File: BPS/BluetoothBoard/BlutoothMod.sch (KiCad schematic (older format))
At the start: 12 parts, among them SW2 SW_DIP_x01, U6 RN4870-V_RM118, U7 MCP100-315D

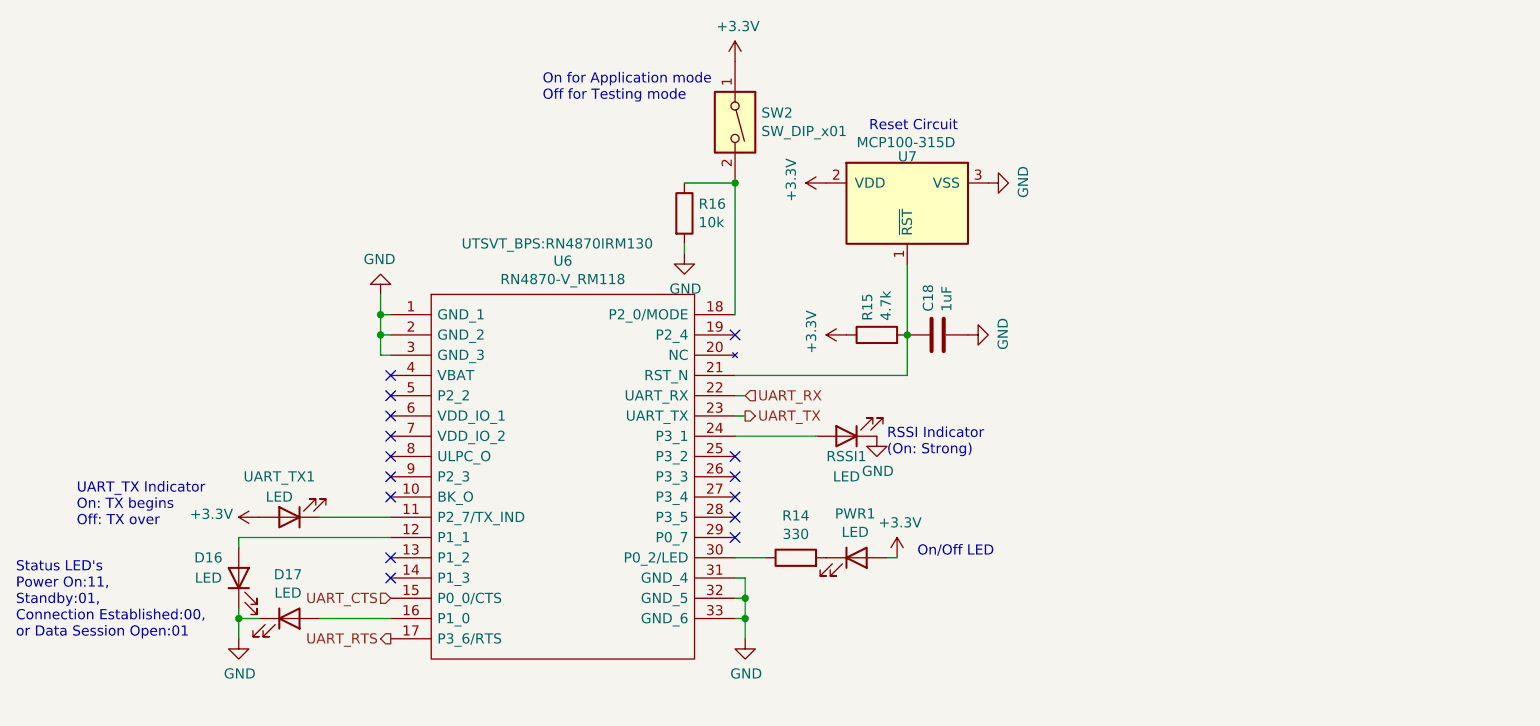
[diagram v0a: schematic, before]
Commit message: Created new board for Bluetooth module because the antenna cannot have a ground plane on it. Made everything connect using pin headers. Will mount the Bluetooth module board onto the Master board.
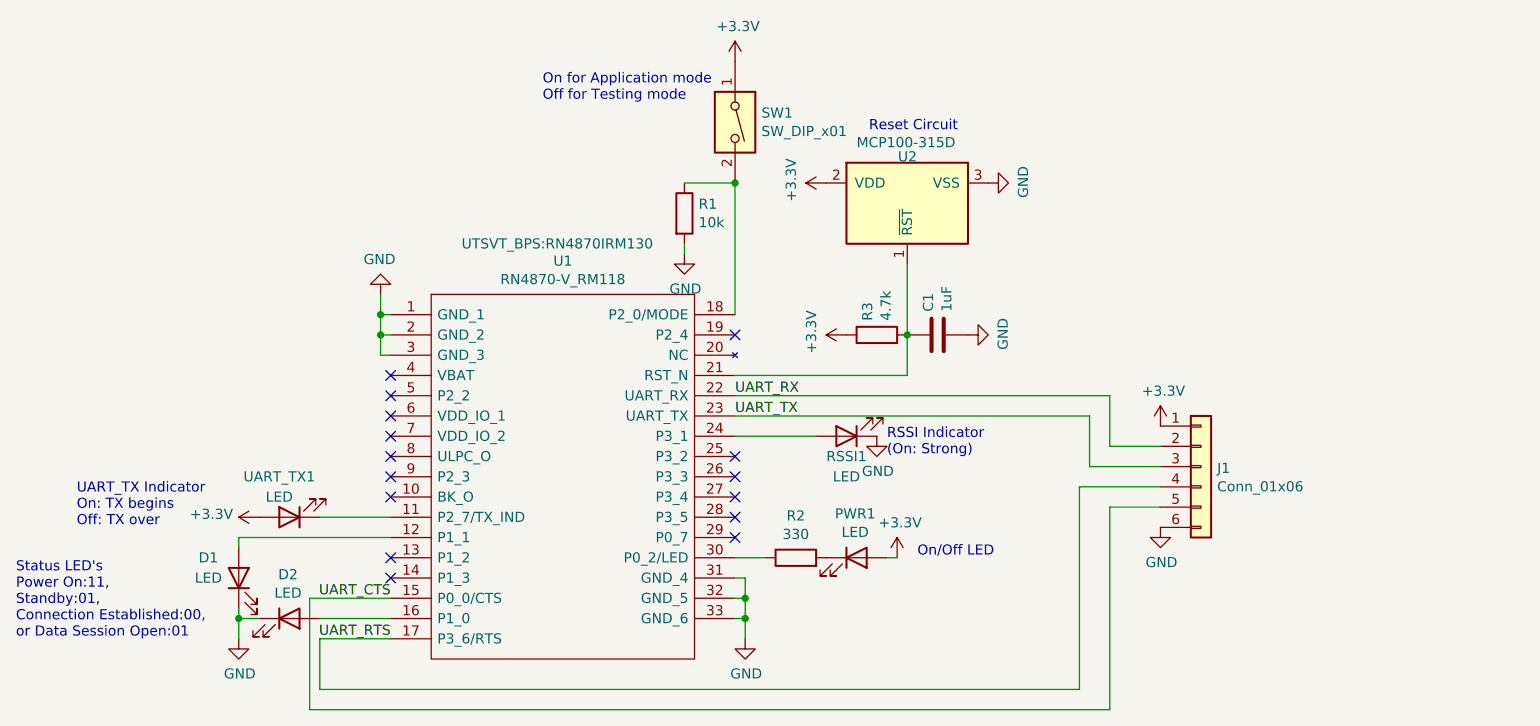
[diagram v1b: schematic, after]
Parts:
- added J1: Conn_01x06, Connector_PinHeader_2.54mm:PinHeader_1x06_P2.54mm_Vertical, symbol Connector_Generic:Conn_01x06
- renumbered C18 to C1, D16 to D1, D17 to D2, R16 to R1, R14 to R2, R15 to R3, SW2 to SW1, U6 to U1, U7 to U2
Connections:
- net +3V3: now also J1.1 (Pin_1)
- net GND: now also J1.6 (Pin_6)
- net UART_CTS: now also J1.5 (Pin_5)
- net UART_RTS: now also J1.4 (Pin_4)
- net UART_RX: now also J1.2 (Pin_2)
- net UART_TX: now also J1.3 (Pin_3)
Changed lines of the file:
@@
 $Descr A4 11693 8268
 encoding utf-8
-Sheet 11 11
+Sheet 1 1
 Title ""
 Date ""
@@
 $EndDescr
 $Comp
-L utsvt-bltmod:RN4870-V_RM118 U6
+L utsvt-bltmod:RN4870-V_RM118 U1
 U 1 1 5EE47912
 P 5000 2900
-F 0 "U6" H 5850 3165 50  0000 C CNN
+F 0 "U1" H 5850 3165 50  0000 C CNN
 F 1 "RN4870-V_RM118" H 5850 3074 50  0000 C CNN
 F 2 "UTSVT_BPS:RN4870IRM130" H 5350 3250 50  0000 L CNN
@@
 Connection ~ 6750 4400
 $Comp
-L power:GND #PWR0106
+L power:GND #PWR06
 U 1 1 5EE48E9A
 P 6750 4500
-F 0 "#PWR0106" H 6750 4250 50  0001 C CNN
+F 0 "#PWR06" H 6750 4250 50  0001 C CNN
 F 1 "GND" H 6755 4327 50  0000 C CNN
 F 2 "" H 6750 4500 50  0001 C CNN
@@
 Connection ~ 4950 2900
 $Comp
-L power:GND #PWR0107
+L power:GND #PWR03
 U 1 1 5EE4937A
 P 4950 2800
-F 0 "#PWR0107" H 4950 2550 50  0001 C CNN
+F 0 "#PWR03" H 4950 2550 50  0001 C CNN
 F 1 "GND" H 4955 2627 50  0000 C CNN
 F 2 "" H 4950 2800 50  0001 C CNN
@@
 $EndComp
 $Comp
-L power:+3.3V #PWR0112
+L power:+3.3V #PWR08
 U 1 1 5EE112CA
 P 7250 3000
-F 0 "#PWR0112" H 7250 2850 50  0001 C CNN
+F 0 "#PWR08" H 7250 2850 50  0001 C CNN
 F 1 "+3.3V" H 7265 3173 50  0000 C CNN
 F 2 "" H 7250 3000 50  0001 C CNN
@@
 $EndComp
 $Comp
-L Device:R R15
+L Device:R R3
 U 1 1 5EE108D1
 P 7400 3000
-F 0 "R15" H 7470 3046 50  0000 L CNN
+F 0 "R3" H 7470 3046 50  0000 L CNN
 F 1 "4.7k" H 7470 2955 50  0000 L CNN
 F 2 "Resistor_SMD:R_0805_2012Metric" V 7330 3000 50  0001 C CNN
@@
 $EndComp
 $Comp
-L Device:C C18
+L Device:C C1
 U 1 1 5EE11D9D
 P 7700 3000
-F 0 "C18" H 7815 3046 50  0000 L CNN
+F 0 "C1" H 7815 3046 50  0000 L CNN
 F 1 "1uF" H 7815 2955 50  0000 L CNN
 F 2 "Capacitor_SMD:C_0805_2012Metric" H 7738 2850 50  0001 C CNN
@@
 Connection ~ 7550 3000
 $Comp
-L power:GND #PWR0113
+L power:GND #PWR011
 U 1 1 5EE12187
 P 7850 3000
-F 0 "#PWR0113" H 7850 2750 50  0001 C CNN
+F 0 "#PWR011" H 7850 2750 50  0001 C CNN
 F 1 "GND" H 7855 2827 50  0000 C CNN
 F 2 "" H 7850 3000 50  0001 C CNN
@@
 	7550 3000 7550 2650
 $Comp
-L power:GND #PWR0114
+L power:GND #PWR012
 U 1 1 5EE1353A
 P 7950 2250
-F 0 "#PWR0114" H 7950 2000 50  0001 C CNN
+F 0 "#PWR012" H 7950 2000 50  0001 C CNN
 F 1 "GND" H 7955 2077 50  0000 C CNN
 F 2 "" H 7950 2250 50  0001 C CNN
@@
 $EndComp
 $Comp
-L power:+3.3V #PWR0115
+L power:+3.3V #PWR07
 U 1 1 5EE13791
 P 7150 2250
-F 0 "#PWR0115" H 7150 2100 50  0001 C CNN
+F 0 "#PWR07" H 7150 2100 50  0001 C CNN
 F 1 "+3.3V" H 7165 2423 50  0000 C CNN
 F 2 "" H 7150 2250 50  0001 C CNN
@@
 $EndComp
 $Comp
-L Device:R R14
+L Device:R R2
 U 1 1 5EE13A0C
 P 7000 4100
-F 0 "R14" V 7207 4100 50  0000 C CNN
+F 0 "R2" V 7207 4100 50  0000 C CNN
 F 1 "330" V 7116 4100 50  0000 C CNN
 F 2 "Resistor_SMD:R_0805_2012Metric" V 6930 4100 50  0001 C CNN
@@
 $EndComp
 $Comp
-L power:+3.3V #PWR0116
+L power:+3.3V #PWR010
 U 1 1 5EE14FBF
 P 7500 4100
-F 0 "#PWR0116" H 7500 3950 50  0001 C CNN
+F 0 "#PWR010" H 7500 3950 50  0001 C CNN
 F 1 "+3.3V" H 7515 4273 50  0000 C CNN
 F 2 "" H 7500 4100 50  0001 C CNN
@@
 NoConn ~ 5000 3600
 NoConn ~ 5000 3300
-Text HLabel 6750 3300 2    50   Input ~ 0
-UART_RX
-Text HLabel 6750 3400 2    50   Output ~ 0
-UART_TX
-$Comp
-L Device:LED D16
+$Comp
+L Device:LED D1
 U 1 1 5EE20E59
 P 4250 4200
-F 0 "D16" V 4350 4350 50  0000 C CNN
+F 0 "D1" V 4350 4350 50  0000 C CNN
 F 1 "LED" V 4250 4350 50  0000 C CNN
 F 2 "LED_SMD:LED_0805_2012Metric" H 4250 4200 50  0001 C CNN
@@
 $EndComp
 $Comp
-L Device:LED D17
+L Device:LED D2
 U 1 1 5EE21939
 P 4500 4400
-F 0 "D17" H 4493 4617 50  0000 C CNN
+F 0 "D2" H 4493 4617 50  0000 C CNN
 F 1 "LED" H 4493 4526 50  0000 C CNN
 F 2 "LED_SMD:LED_0805_2012Metric" H 4500 4400 50  0001 C CNN
@@
 $EndComp
 $Comp
-L power:GND #PWR0117
+L power:GND #PWR01
 U 1 1 5EE2468E
 P 4250 4500
-F 0 "#PWR0117" H 4250 4250 50  0001 C CNN
+F 0 "#PWR01" H 4250 4250 50  0001 C CNN
 F 1 "GND" H 4255 4327 50  0000 C CNN
 F 2 "" H 4250 4500 50  0001 C CNN
@@
 Text Notes 7800 2000 2    50   ~ 0
 Reset Circuit\n
-Wire Wire Line
-	6700 3300 6750 3300
-Wire Wire Line
-	6700 3400 6750 3400
-$Comp
-L Power_Supervisor:MCP100-315D U7
+$Comp
+L Power_Supervisor:MCP100-315D U2
 U 1 1 5EE0F520
 P 7550 2350
-F 0 "U7" V 7320 2396 50  0000 R CNN
+F 0 "U2" V 7320 2396 50  0000 R CNN
 F 1 "MCP100-315D" V 7250 2600 50  0000 R CNN
 F 2 "UTSVT_BPS:SOT96P240X110-3N" H 7150 2500 50  0001 C CNN
@@
 $EndComp
 $Comp
-L power:GND #PWR033
+L power:GND #PWR09
 U 1 1 5EE552B9
 P 7400 3500
-F 0 "#PWR033" H 7400 3250 50  0001 C CNN
+F 0 "#PWR09" H 7400 3250 50  0001 C CNN
 F 1 "GND" H 7405 3327 50  0000 C CNN
 F 2 "" H 7400 3500 50  0001 C CNN
@@
 $EndComp
 $Comp
-L power:+3.3V #PWR028
+L power:+3.3V #PWR02
 U 1 1 5EE5298C
 P 4350 3900
-F 0 "#PWR028" H 4350 3750 50  0001 C CNN
+F 0 "#PWR02" H 4350 3750 50  0001 C CNN
 F 1 "+3.3V" V 4365 4028 50  0000 L CNN
 F 2 "" H 4350 3900 50  0001 C CNN
@@
 UART_TX Indicator\nOn: TX begins\nOff: TX over
 $Comp
-L Switch:SW_DIP_x01 SW2
+L Switch:SW_DIP_x01 SW1
 U 1 1 5EE36BE3
 P 6700 1950
-F 0 "SW2" V 6654 2080 50  0000 L CNN
+F 0 "SW1" V 6654 2080 50  0000 L CNN
 F 1 "SW_DIP_x01" V 6745 2080 50  0000 L CNN
 F 2 "Button_Switch_SMD:SW_DIP_SPSTx01_Slide_6.7x4.1mm_W6.73mm_P2.54mm_LowProfile_JPin" H 6700 1950 50  0001 C CNN
@@
 $EndComp
 $Comp
-L power:+3.3V #PWR035
+L power:+3.3V #PWR05
 U 1 1 5EE37A78
 P 6700 1650
-F 0 "#PWR035" H 6700 1500 50  0001 C CNN
+F 0 "#PWR05" H 6700 1500 50  0001 C CNN
 F 1 "+3.3V" H 6715 1823 50  0000 C CNN
 F 2 "" H 6700 1650 50  0001 C CNN
@@
 $EndComp
 $Comp
-L power:GND #PWR034
+L power:GND #PWR04
 U 1 1 5EE37E2D
 P 6450 2600
-F 0 "#PWR034" H 6450 2350 50  0001 C CNN
+F 0 "#PWR04" H 6450 2350 50  0001 C CNN
 F 1 "GND" H 6455 2427 50  0000 C CNN
 F 2 "" H 6450 2600 50  0001 C CNN
@@
 $EndComp
 $Comp
-L Device:R R16
+L Device:R R1
 U 1 1 5EE38412
 P 6450 2400
-F 0 "R16" H 6520 2446 50  0000 L CNN
+F 0 "R1" H 6520 2446 50  0000 L CNN
 F 1 "10k" H 6520 2355 50  0000 L CNN
 F 2 "Resistor_SMD:R_0805_2012Metric" V 6380 2400 50  0001 C CNN
@@
 Wire Wire Line
 	4650 4400 5000 4400
-Text HLabel 5000 4300 0    50   Input ~ 0
-UART_CTS
-Text HLabel 5000 4500 0    50   Output ~ 0
-UART_RTS
 NoConn ~ 5000 3500
 NoConn ~ 5000 3400
 NoConn ~ 5000 3200
+Wire Wire Line
+	8550 3300 8550 3550
+Wire Wire Line
+	6700 3300 8550 3300
+Wire Wire Line
+	8450 3400 8450 3650
+Wire Wire Line
+	6700 3400 8450 3400
+Text Label 6700 3300 0    50   ~ 0
+UART_RX
+Text Label 6700 3400 0    50   ~ 0
+UART_TX
+Text Label 5000 4300 2    50   ~ 0
+UART_CTS
+Text Label 5000 4500 2    50   ~ 0
+UART_RTS
+Wire Wire Line
+	5000 4300 4600 4300
+Wire Wire Line
+	4600 4300 4600 4850
+Wire Wire Line
+	4600 4850 8550 4850
+Wire Wire Line
+	8550 4850 8550 3850
+Wire Wire Line
+	5000 4500 4650 4500
+Wire Wire Line
+	4650 4500 4650 4750
+Wire Wire Line
+	4650 4750 8400 4750
+Wire Wire Line
+	8400 4750 8400 3750
+$Comp
+L Connector_Generic:Conn_01x06 J1
+U 1 1 5EF85BFE
+P 9000 3650
+F 0 "J1" H 9080 3642 50  0000 L CNN
+F 1 "Conn_01x06" H 9080 3551 50  0000 L CNN
+F 2 "Connector_PinHeader_2.54mm:PinHeader_1x06_P2.54mm_Vertical" H 9000 3650 50  0001 C CNN
+F 3 "~" H 9000 3650 50  0001 C CNN
+	1    9000 3650
+	1    0    0    -1
+$EndComp
+Wire Wire Line
+	8550 3850 8800 3850
+Wire Wire Line
+	8400 3750 8800 3750
+Wire Wire Line
+	8450 3650 8800 3650
+Wire Wire Line
+	8550 3550 8800 3550
+$Comp
+L power:+3.3V #PWR0101
+U 1 1 5EF898CE
+P 8800 3450
+F 0 "#PWR0101" H 8800 3300 50  0001 C CNN
+F 1 "+3.3V" H 8815 3623 50  0000 C CNN
+F 2 "" H 8800 3450 50  0001 C CNN
+F 3 "" H 8800 3450 50  0001 C CNN
+	1    8800 3450
+	1    0    0    -1
+$EndComp
+$Comp
+L power:GND #PWR0102
+U 1 1 5EF89C20
+P 8800 3950
+F 0 "#PWR0102" H 8800 3700 50  0001 C CNN
+F 1 "GND" H 8805 3777 50  0000 C CNN
+F 2 "" H 8800 3950 50  0001 C CNN
+F 3 "" H 8800 3950 50  0001 C CNN
+	1    8800 3950
+	1    0    0    -1
+$EndComp
 $EndSCHEMATC

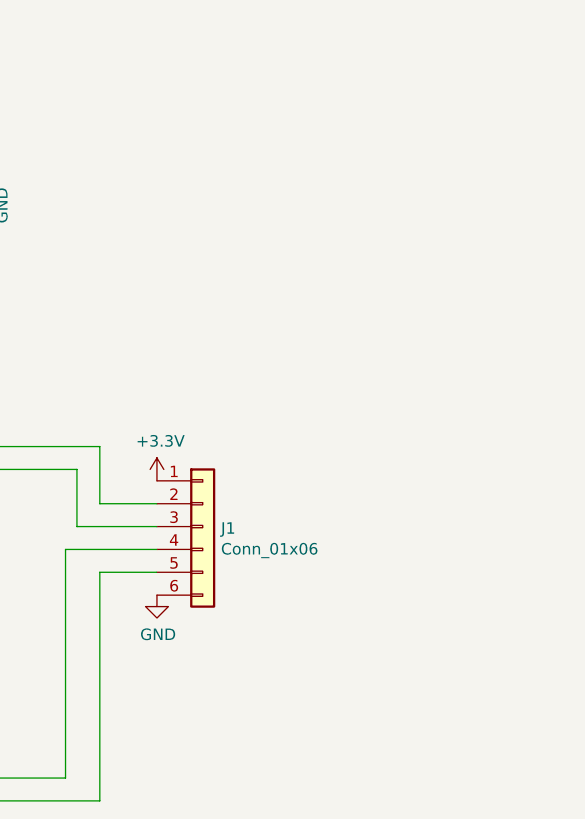
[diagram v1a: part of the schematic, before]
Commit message: Finished master board. Working to make sure that bluetooth mount won't cover anything important on master board, yet still be big enough to hold everything.
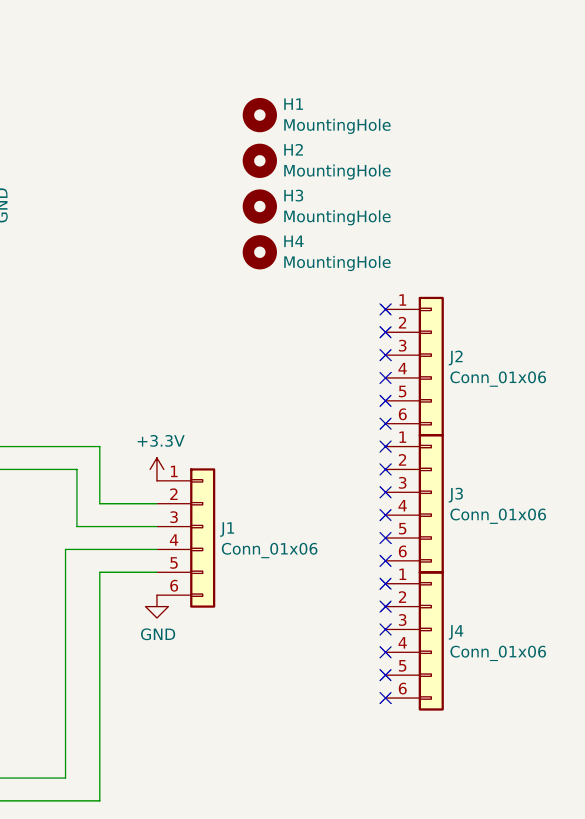
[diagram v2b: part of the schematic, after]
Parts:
- added H1, H2, H3, H4: MountingHole, MountingHole:MountingHole_2.1mm, symbol Mechanical:MountingHole
- added J2, J3, J4: Conn_01x06, Connector_PinSocket_2.54mm:PinSocket_1x06_P2.54mm_Vertical, symbol Connector_Generic:Conn_01x06
- J1: footprint Connector_PinHeader_2.54mm:PinHeader_1x06_P2.54mm_Vertical -> Connector_PinSocket_2.54mm:PinSocket_1x06_P2.54mm_Vertical
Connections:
- no-connect marks 15 -> 33
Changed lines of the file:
@@
 F 0 "J1" H 9080 3642 50  0000 L CNN
 F 1 "Conn_01x06" H 9080 3551 50  0000 L CNN
-F 2 "Connector_PinHeader_2.54mm:PinHeader_1x06_P2.54mm_Vertical" H 9000 3650 50  0001 C CNN
+F 2 "Connector_PinSocket_2.54mm:PinSocket_1x06_P2.54mm_Vertical" H 9000 3650 50  0001 C CNN
 F 3 "~" H 9000 3650 50  0001 C CNN
 	1    9000 3650
@@
 	1    0    0    -1
 $EndComp
+$Comp
+L Mechanical:MountingHole H2
+U 1 1 5EFE54EF
+P 9250 2050
+F 0 "H2" H 9350 2096 50  0000 L CNN
+F 1 "MountingHole" H 9350 2005 50  0000 L CNN
+F 2 "MountingHole:MountingHole_2.1mm" H 9250 2050 50  0001 C CNN
+F 3 "~" H 9250 2050 50  0001 C CNN
+	1    9250 2050
+	1    0    0    -1
+$EndComp
+$Comp
+L Mechanical:MountingHole H3
+U 1 1 5EFE6AD0
+P 9250 2250
+F 0 "H3" H 9350 2296 50  0000 L CNN
+F 1 "MountingHole" H 9350 2205 50  0000 L CNN
+F 2 "MountingHole:MountingHole_2.1mm" H 9250 2250 50  0001 C CNN
+F 3 "~" H 9250 2250 50  0001 C CNN
+	1    9250 2250
+	1    0    0    -1
+$EndComp
+$Comp
+L Mechanical:MountingHole H4
+U 1 1 5EFE6EF1
+P 9250 2450
+F 0 "H4" H 9350 2496 50  0000 L CNN
+F 1 "MountingHole" H 9350 2405 50  0000 L CNN
+F 2 "MountingHole:MountingHole_2.1mm" H 9250 2450 50  0001 C CNN
+F 3 "~" H 9250 2450 50  0001 C CNN
+	1    9250 2450
+	1    0    0    -1
+$EndComp
+$Comp
+L Mechanical:MountingHole H1
+U 1 1 5EFE71CA
+P 9250 1850
+F 0 "H1" H 9350 1896 50  0000 L CNN
+F 1 "MountingHole" H 9350 1805 50  0000 L CNN
+F 2 "MountingHole:MountingHole_2.1mm" H 9250 1850 50  0001 C CNN
+F 3 "~" H 9250 1850 50  0001 C CNN
+	1    9250 1850
+	1    0    0    -1
+$EndComp
+$Comp
+L Connector_Generic:Conn_01x06 J3
+U 1 1 5EFE794B
+P 10000 3500
+F 0 "J3" H 10080 3492 50  0000 L CNN
+F 1 "Conn_01x06" H 10080 3401 50  0000 L CNN
+F 2 "Connector_PinSocket_2.54mm:PinSocket_1x06_P2.54mm_Vertical" H 10000 3500 50  0001 C CNN
+F 3 "~" H 10000 3500 50  0001 C CNN
+	1    10000 3500
+	1    0    0    -1
+$EndComp
+$Comp
+L Connector_Generic:Conn_01x06 J4
+U 1 1 5EFE8081
+P 10000 4100
+F 0 "J4" H 10080 4092 50  0000 L CNN
+F 1 "Conn_01x06" H 10080 4001 50  0000 L CNN
+F 2 "Connector_PinSocket_2.54mm:PinSocket_1x06_P2.54mm_Vertical" H 10000 4100 50  0001 C CNN
+F 3 "~" H 10000 4100 50  0001 C CNN
+	1    10000 4100
+	1    0    0    -1
+$EndComp
+$Comp
+L Connector_Generic:Conn_01x06 J2
+U 1 1 5EFE9541
+P 10000 2900
+F 0 "J2" H 10080 2892 50  0000 L CNN
+F 1 "Conn_01x06" H 10080 2801 50  0000 L CNN
+F 2 "Connector_PinSocket_2.54mm:PinSocket_1x06_P2.54mm_Vertical" H 10000 2900 50  0001 C CNN
+F 3 "~" H 10000 2900 50  0001 C CNN
+	1    10000 2900
+	1    0    0    -1
+$EndComp
+NoConn ~ 9800 2700
+NoConn ~ 9800 2800
+NoConn ~ 9800 2900
+NoConn ~ 9800 3000
+NoConn ~ 9800 3100
+NoConn ~ 9800 3200
+NoConn ~ 9800 3300
+NoConn ~ 9800 3400
+NoConn ~ 9800 3500
+NoConn ~ 9800 3600
+NoConn ~ 9800 3700
+NoConn ~ 9800 3800
+NoConn ~ 9800 3900
+NoConn ~ 9800 4000
+NoConn ~ 9800 4100
+NoConn ~ 9800 4200
+NoConn ~ 9800 4300
+NoConn ~ 9800 4400
 $EndSCHEMATC

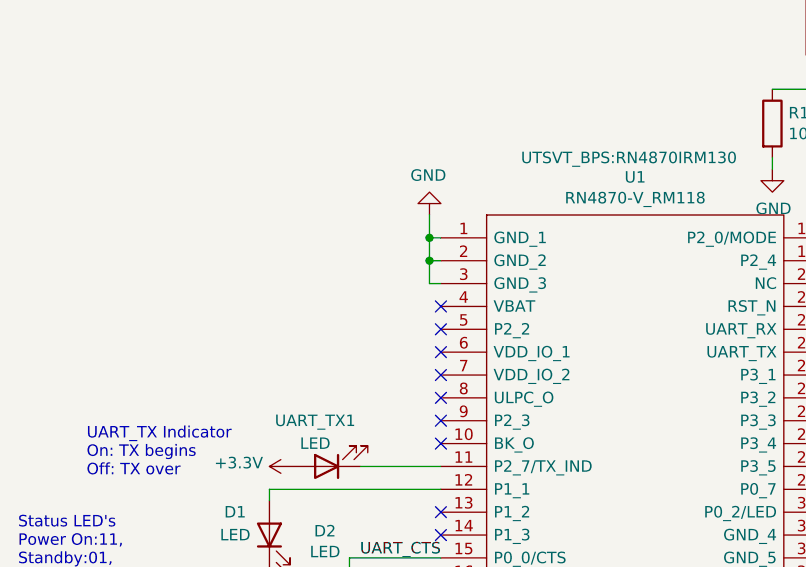
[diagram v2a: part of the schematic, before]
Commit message: Connected power to Bluetooth Module
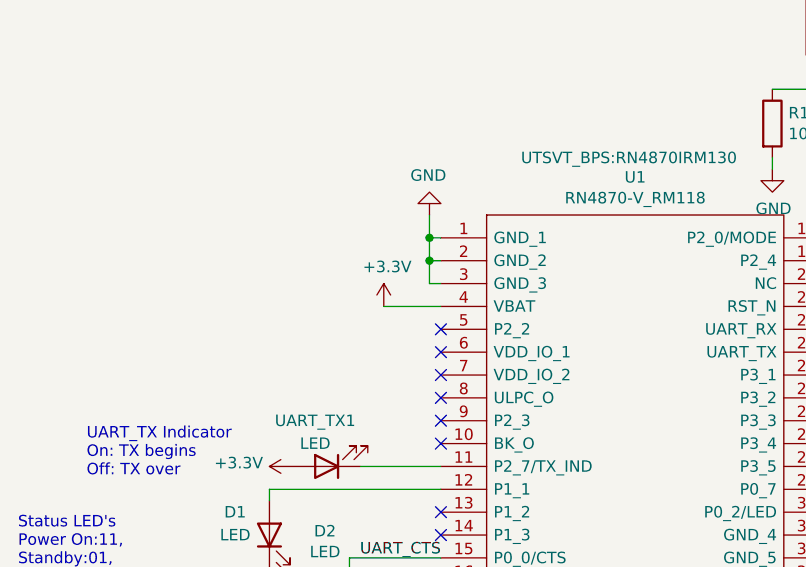
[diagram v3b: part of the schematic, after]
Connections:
- net +3V3: now also U1.4 (VBAT)
- no-connect marks 33 -> 32
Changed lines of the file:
@@
 NoConn ~ 5000 3500
 NoConn ~ 5000 3400
-NoConn ~ 5000 3200
 Wire Wire Line
 	8550 3300 8550 3550
@@
 NoConn ~ 9800 4300
 NoConn ~ 9800 4400
+$Comp
+L power:+3.3V #PWR?
+U 1 1 5EFF4B60
+P 4750 3200
+F 0 "#PWR?" H 4750 3050 50  0001 C CNN
+F 1 "+3.3V" H 4765 3373 50  0000 C CNN
+F 2 "" H 4750 3200 50  0001 C CNN
+F 3 "" H 4750 3200 50  0001 C CNN
+	1    4750 3200
+	1    0    0    -1
+$EndComp
+Wire Wire Line
+	4750 3200 5000 3200
 $EndSCHEMATC
